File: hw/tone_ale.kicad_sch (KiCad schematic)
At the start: 51 parts, among them J1 Conn_01x02, J2 USB_B_Micro, J3 Conn_01x02, J4 Conn_02x08_Odd_Even, J5 Conn_02x11_Odd_Even, U1 NCP1117-3.3_SOT223, U2 W25Q128JVS, U3 RP2040, U4 PCM5102, U5 PCM1808PWR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

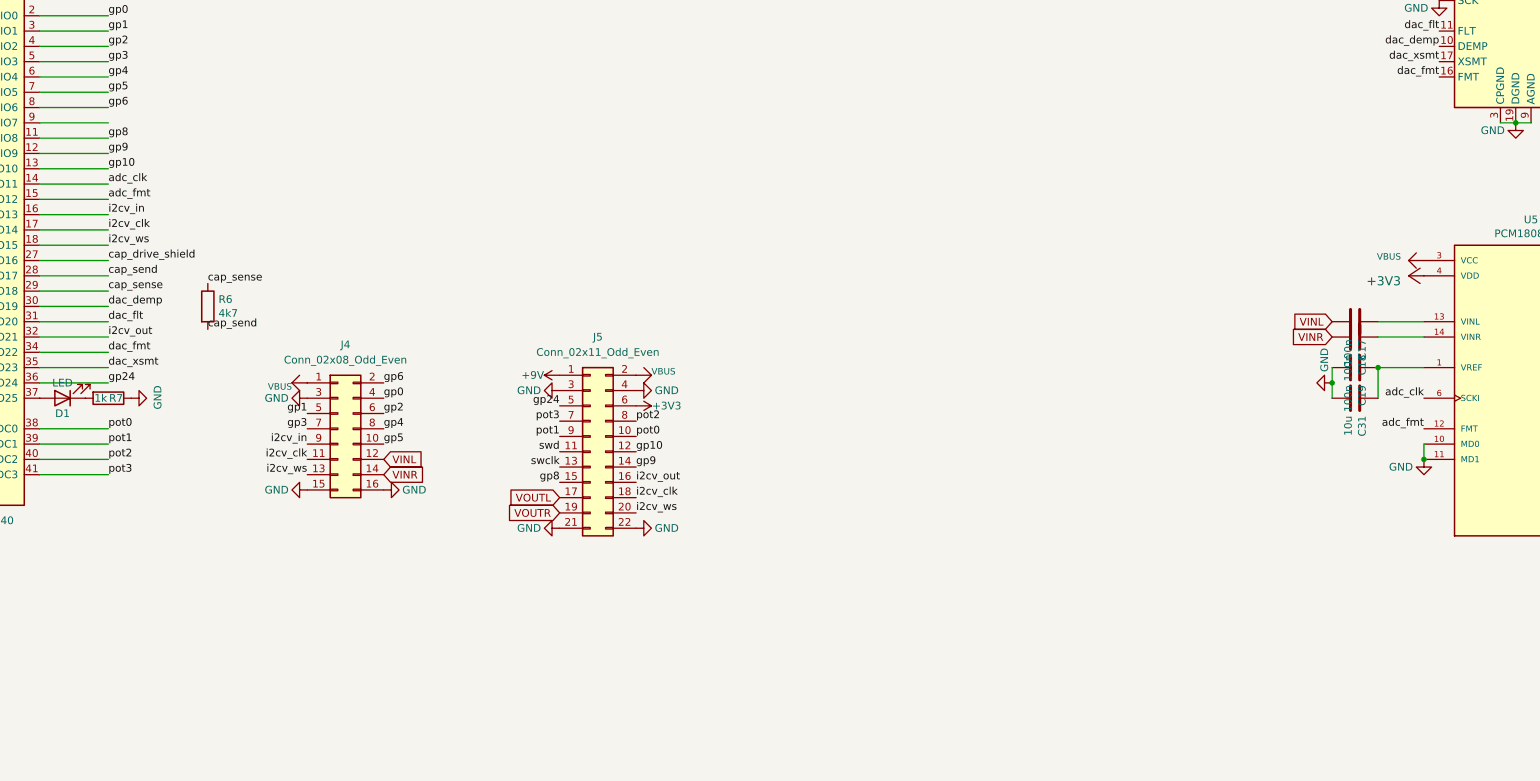
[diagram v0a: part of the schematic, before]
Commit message: Updated hardware. Made wah only engaged while foot is on pedal
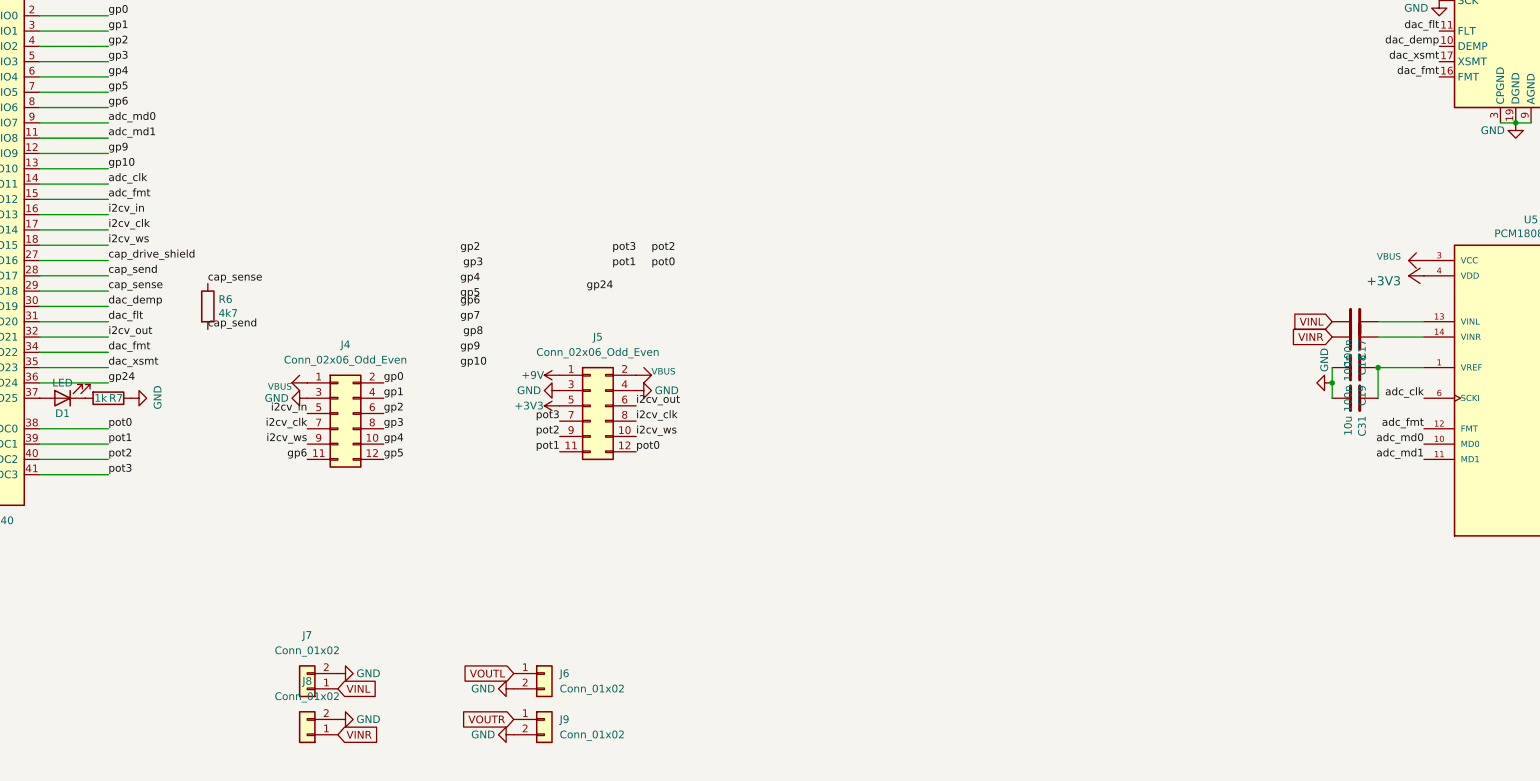
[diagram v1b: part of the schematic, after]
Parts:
- removed J4: Conn_02x08_Odd_Even, Connector_PinHeader_2.54mm:PinHeader_2x08_P2.54mm_Vertical, symbol Connector_Generic:Conn_02x08_Odd_Even
- removed J5: Conn_02x11_Odd_Even, Connector_PinHeader_2.54mm:PinHeader_2x11_P2.54mm_Vertical, symbol Connector_Generic:Conn_02x11_Odd_Even
- added J4, J5: Conn_02x06_Odd_Even, Connector_PinHeader_2.54mm:PinHeader_2x06_P2.54mm_Vertical, symbol Connector_Generic:Conn_02x06_Odd_Even
- added J6, J7, J8, J9: Conn_01x02, mylib:acjm_mhdr, symbol Connector_Generic:Conn_01x02
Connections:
- net +3V3: now also J5.5 (Pin_5)
- net +9V: now also J5.1 (Pin_1)
- net GND: now also J4.3 (Pin_3), J5.3 (Pin_3), J5.4 (Pin_4), J6.2 (Pin_2), J7.2 (Pin_2), J8.2 (Pin_2), J9.2 (Pin_2); no longer U5.10 (MD0), U5.11 (MD1)
- net VBUS: now also J4.1 (Pin_1), J5.2 (Pin_2)
- net VINL: now also J7.1 (Pin_1)
- net VINR: now also J8.1 (Pin_1)
- net VOUTL: now also J6.1 (Pin_1)
- net VOUTR: now also J9.1 (Pin_1)
- net gp0: now also J4.2 (Pin_2)
- net gp1: now also J4.4 (Pin_4)
- net gp2: now also J4.6 (Pin_6)
- net gp3: now also J4.8 (Pin_8)
- net gp4: now also J4.10 (Pin_10)
- net gp5: now also J4.12 (Pin_12)
- net gp6: now also J4.11 (Pin_11)
- net gp8: no longer U3.11 (GPIO8)
- net i2cv_clk: now also J4.7 (Pin_7), J5.8 (Pin_8)
- net i2cv_in: now also J4.5 (Pin_5)
- net i2cv_out: now also J5.6 (Pin_6)
- net i2cv_ws: now also J4.9 (Pin_9), J5.10 (Pin_10)
- net pot0: now also J5.12 (Pin_12)
- net pot1: now also J5.11 (Pin_11)
- net pot2: now also J5.9 (Pin_9)
- net pot3: now also J5.7 (Pin_7)
- net adc_md0: now reaches U3.9 (GPIO7)
- net adc_md0: now also U5.10 (MD0)
- new net adc_md1: U3.11 (GPIO8), U5.11 (MD1)
